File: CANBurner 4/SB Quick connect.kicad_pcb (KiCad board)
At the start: 2 copper layers, 33.8 x 30 mm, 9 parts

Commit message: rev 4 changes
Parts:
- added R Bypass: LED Bypass, Jumper:SolderJumper-2_P1.3mm_Open_TrianglePad1.0x1.5mm, B.Cu at (71.3, 27.9)
- added R1: R, Resistor_THT:R_Axial_DIN0414_L11.9mm_D4.5mm_P15.24mm_Horizontal, F.Cu at (82.8, 28.0)
- moved G*** 18.4 mm to (87.0, 27.6)
- moved G*** 16.1 mm to (86.9, 27.6)
- moved Toolboard 1.37 mm to (91.5, 39.4)
- renumbered Stealthburner to J1
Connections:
- J1 pad 3: /HEF -> Net-(J1-Pad3)
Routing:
- net Net-(J1-Pad3): track 0.00 -> 13.8 mm
- net /HEF: track 8.92 -> 20.6 mm
- net /A2: track 44.8 -> 38.4 mm
- net /5V: track 49.7 -> 46.9 mm
- net /A1: track 31.0 -> 29.0 mm
- net /24V: track 17.5 -> 18.9 mm
- net /GND: track 56.6 -> 55.6 mm
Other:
- board text added: "v4"
- board text removed: "v3"

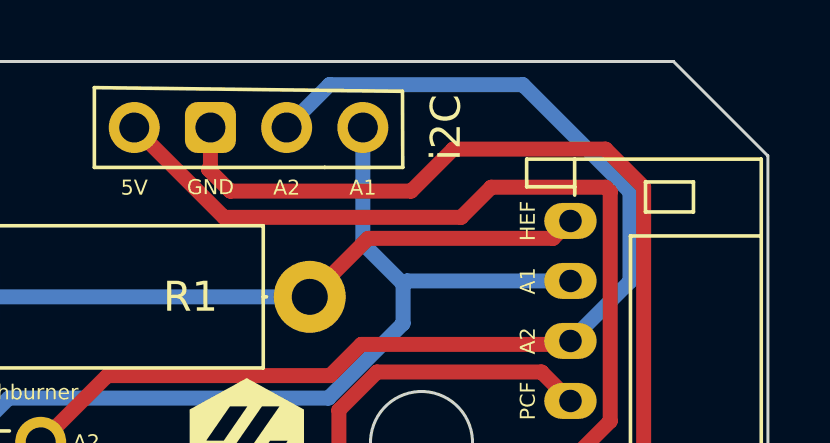
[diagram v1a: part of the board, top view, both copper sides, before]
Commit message: Fixed Net Trace on resistor for v4
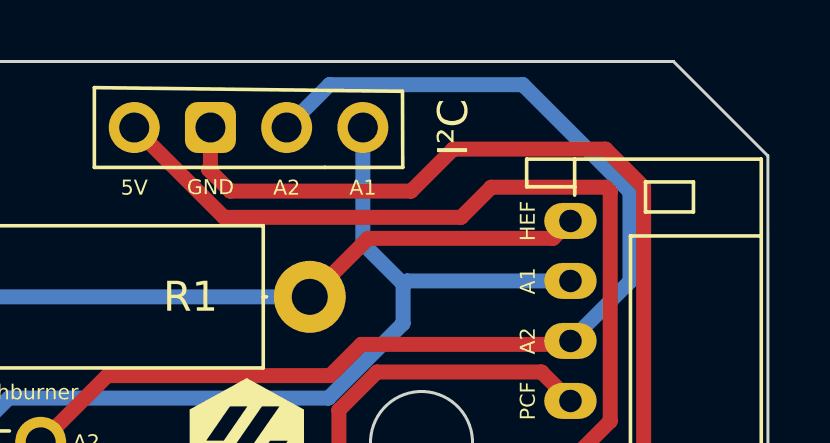
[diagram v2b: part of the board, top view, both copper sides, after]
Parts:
- renumbered i2C to I²C
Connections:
- J1 pad 3: Net-(J1-Pad3) -> /HEF
- R Bypass pad 2: Net-(J1-Pad3) -> /HEF
- R1 pad 2: Net-(J1-Pad3) -> /HEF
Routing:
- net /HEF: track 20.6 -> 34.4 mm
- net Net-(J1-Pad3): track 13.8 -> 0.00 mm
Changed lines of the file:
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@@
   (net 7 "/5V")
   (net 8 "/GND")
-  (net 9 "Net-(J1-Pad3)")
   (footprint "Connector_PinSocket_2.54mm:PinSocket_1x04_P2.54mm_Vertical" (layer "F.Cu")
     (at 84.619469 22.330407 -90)
@@
     (tags "Through hole socket strip THT 1x04 2.54mm single row")
     (attr through_hole)
-    (fp_text reference "i2C" (at 0 -2.77 -90) (layer "F.SilkS")
+    (fp_text reference "I²C" (at 0 -3.010531 -90) (layer "F.SilkS")
       (effects (font (size 1 1) (thickness 0.15)))
     )
@@
       (net 2 "/HEF") (pintype "passive"))
     (pad "2" thru_hole oval (at 15.24 0 180) (size 2.4 2.4) (drill 1.2) (layers *.Cu *.Mask)
-      (net 9 "Net-(J1-Pad3)") (pintype "passive"))
+      (net 2 "/HEF") (pintype "passive"))
     (model "${KICAD6_3DMODEL_DIR}/Resistor_THT.3dshapes/R_Axial_DIN0414_L11.9mm_D4.5mm_P15.24mm_Horizontal.wrl"
       (offset (xyz 0 0 0))
@@
       (net 4 "/A2") (pinfunction "Pin_2") (pintype "passive"))
     (pad "3" thru_hole oval (at 8.08 2.54 180) (size 1.7 1.7) (drill 1) (layers *.Cu *.Mask)
-      (net 9 "Net-(J1-Pad3)") (pinfunction "Pin_3") (pintype "passive"))
+      (net 2 "/HEF") (pinfunction "Pin_3") (pintype "passive"))
     (pad "4" thru_hole oval (at 10.62 2.54 180) (size 1.7 1.7) (drill 1) (layers *.Cu *.Mask)
       (net 5 "/PCF") (pinfunction "Pin_4") (pintype "passive"))
@@
       ))
     (pad "2" smd custom (at 0.725 0 180) (size 0.3 0.3) (layers "B.Cu" "B.Mask")
-      (net 9 "Net-(J1-Pad3)") (zone_connect 2)
+      (net 2 "/HEF") (zone_connect 2)
       (options (clearance outline) (anchor rect))
       (primitives
@@
       (effects (font (size 1 1) (thickness 0.15)) (justify mirror))
     )
+    (fp_line (start -1.4 1) (end 1.4 1) (layer "B.SilkS") (width 0.12))
     (fp_line (start 1.4 -1) (end -1.4 -1) (layer "B.SilkS") (width 0.12))
-    (fp_line (start -1.4 1) (end 1.4 1) (layer "B.SilkS") (width 0.12))
     (fp_line (start 1.4 1) (end 1.4 -1) (layer "B.SilkS") (width 0.12))
     (fp_line (start -1.4 -1) (end -1.4 1) (layer "B.SilkS") (width 0.12))
+    (fp_line (start 1.65 -1.25) (end 1.65 1.25) (layer "B.CrtYd") (width 0.05))
+    (fp_line (start -1.65 1.25) (end -1.65 -1.25) (layer "B.CrtYd") (width 0.05))
     (fp_line (start 1.65 -1.25) (end -1.65 -1.25) (layer "B.CrtYd") (width 0.05))
-    (fp_line (start -1.65 1.25) (end -1.65 -1.25) (layer "B.CrtYd") (width 0.05))
-    (fp_line (start 1.65 -1.25) (end 1.65 1.25) (layer "B.CrtYd") (width 0.05))
     (fp_line (start -1.65 1.25) (end 1.65 1.25) (layer "B.CrtYd") (width 0.05))
     (pad "1" smd custom (at -0.725 0 180) (size 0.3 0.3) (layers "B.Cu" "B.Mask")
@@
   (segment (start 76.766341 37.56) (end 73.881315 40.445026) (width 0.5) (layer "B.Cu") (net 1))
   (segment (start 91.425 37.56) (end 76.766341 37.56) (width 0.5) (layer "B.Cu") (net 1))
+  (segment (start 67.61 34.885) (end 67.61 27.975) (width 0.5) (layer "F.Cu") (net 2))
   (segment (start 90.96 26.025) (end 84.8 26.025) (width 0.5) (layer "F.Cu") (net 2))
   (segment (start 84.8 26.025) (end 82.85 27.975) (width 0.5) (layer "F.Cu") (net 2))
   (segment (start 91.54 25.445) (end 90.96 26.025) (width 0.5) (layer "F.Cu") (net 2))
+  (segment (start 71.341315 35.365026) (end 68.090026 35.365026) (width 0.5) (layer "F.Cu") (net 2))
+  (segment (start 68.090026 35.365026) (end 67.61 34.885) (width 0.5) (layer "F.Cu") (net 2))
   (segment (start 72.075 27.975) (end 82.85 27.975) (width 0.5) (layer "B.Cu") (net 2))
   (segment (start 72.025 27.925) (end 72.075 27.975) (width 0.5) (layer "B.Cu") (net 2))
+  (segment (start 67.61 27.975) (end 70.525 27.975) (width 0.5) (layer "B.Cu") (net 2))
+  (segment (start 70.525 27.975) (end 70.575 27.925) (width 0.5) (layer "B.Cu") (net 2))
   (segment (start 84.619469 22.330407) (end 84.619469 26.199469) (width 0.5) (layer "B.Cu") (net 3))
   (segment (start 85.96 28.865) (end 85.96 27.58) (width 0.5) (layer "B.Cu") (net 3))
@@
   (segment (start 90.17 39.56) (end 91.425 39.56) (width 0.5) (layer "F.Cu") (net 8))
   (segment (start 72.693145 42.1) (end 71.341315 40.74817) (width 0.5) (layer "F.Cu") (net 8))
-  (segment (start 67.61 34.885) (end 67.61 27.975) (width 0.5) (layer "F.Cu") (net 9))
-  (segment (start 71.341315 35.365026) (end 68.090026 35.365026) (width 0.5) (layer "F.Cu") (net 9))
-  (segment (start 68.090026 35.365026) (end 67.61 34.885) (width 0.5) (layer "F.Cu") (net 9))
-  (segment (start 67.61 27.975) (end 70.525 27.975) (width 0.5) (layer "B.Cu") (net 9))
-  (segment (start 70.525 27.975) (end 70.575 27.925) (width 0.5) (layer "B.Cu") (net 9))
   (group "Toolboard" (id 2335667d-002b-4072-a01c-006de069bb27)
     (members
@@
     )
   )
-  (group "Stealthburner" (id 84d91e41-8b5f-4f18-999f-8d0881376fac)
-    (members
-      0cc294d4-8174-40cd-adae-1c669fb20ee6
-      33876f84-d311-4544-ad87-0757033ad203
-      38a722b5-b3a7-44fa-9fd3-810963860f6d
-      61dff1f2-daa9-4c42-8085-d39a4ca13924
-      68b1b27d-8d64-4433-9e3d-0dcb13da21e0
-      6dbfcb5c-14d4-482d-9ced-bd6a7b50243b
-      8186e727-a0ff-481a-89a5-ac2fd18c164d
-      9c8083f2-e8c2-4287-ba3f-95285f9ed896
-      a07e90e8-3703-4539-96d6-4fb28feac1f2
-      a26d85cd-2996-4a67-b732-66f4757e6a7f
-      ac6060c0-c9e4-4f25-a0cd-a9b31cd09fda
-      c8ee0f48-0e2f-4eb6-9e31-a480bdcd9b27
-      cb8464d4-d5e2-478b-919e-34d2d9a3af95
-      d69232dc-b6e3-4c7a-83d8-4438e28076c1
-      d6c84b52-c5b0-4347-9763-026363551358
-      da5f626d-f178-4627-a86d-2fc98f42ccb3
-      dabf6b38-5f92-46a4-a2d1-cda354ff6934
-      f31c7371-161b-4344-a544-e22115731220
-      f7b762ea-3872-4d70-bf54-d2f9edd1a3c7
-      ffffffff-ffff-ffff-ffff-ffffffffffff
-      ffffffff-ffff-ffff-ffff-ffffffffffff
-    )
-  )

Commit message: Fixed solder mask logos over traces
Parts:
- moved G*** 16.4 mm to (71.1, 22.9)
- moved G*** 9.18 mm to (94.0, 21.6)
